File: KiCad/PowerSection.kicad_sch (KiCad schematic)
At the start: 0 parts

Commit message: Partition schematic to different sheets
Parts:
- added C1, C11, C12, C2, C3, C4, C5, C6, C7: C, symbol Device:C
- added D1: 1N5819, Diode_THT:D_DO-41_SOD81_P10.16mm_Horizontal, symbol Diode:1N5819
- added L1: L, symbol Device:L
- added R1, R2, R3: R, symbol Device:R
- added U2: LM7805_TO220, Package_TO_SOT_THT:TO-220-3_Vertical, symbol Regulator_Linear:LM7805_TO220
- added U4: LM7910_TO220, Package_TO_SOT_THT:TO-220-3_Vertical, symbol Regulator_Linear:LM7910_TO220
- added U6: MC34063AP, Package_DIP:DIP-8_W7.62mm_Socket_LongPads, symbol Regulator_Switching:MC34063AP
- added U7: LM7810_TO220, Package_TO_SOT_THT:TO-220-3_Vertical, symbol Regulator_Linear:LM7810_TO220
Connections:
- new net: D1.1 (K), L1.1, U6.2 (SwE)
- new net: C4.1, U6.3 (TC)
- new net: R1.2, U6.1 (SwC), U6.7 (Ipk), U6.8 (DC)
- new net: R2.2, R3.1, U6.5 (Vfb)
- new net +10V: C12.1, U7.3 (VO)
- new net +12V: C2.1, C3.1, C7.1, R1.1, U2.1 (VI), U6.6 (Vin), U7.1 (VI)
- new net +5V: C5.1, U2.3 (VO)
- new net -10V: C6.2, U4.3 (VO)
- new net -12V: C1.2, C11.2, C4.2, D1.2 (A), R2.1, U4.2 (VI), U6.4 (GND)
- new net GND: C1.1, C11.1, C12.2, C2.2, C3.2, C5.2, C6.1, C7.2, L1.2, R3.2, U2.2 (GND), U4.1 (GND), U7.2 (GND)
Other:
- note added: "5V Logic Stabilizer"
- note added: "Author:"
- note added: "Blazej Chodorowski"
- note added: "Invrting DC-DC coverter"
- note added: "Negative Supply Stabilizer"
- note added: "Positive Supply Stabilizer"
- note added: "Power convertion and stabilization module"

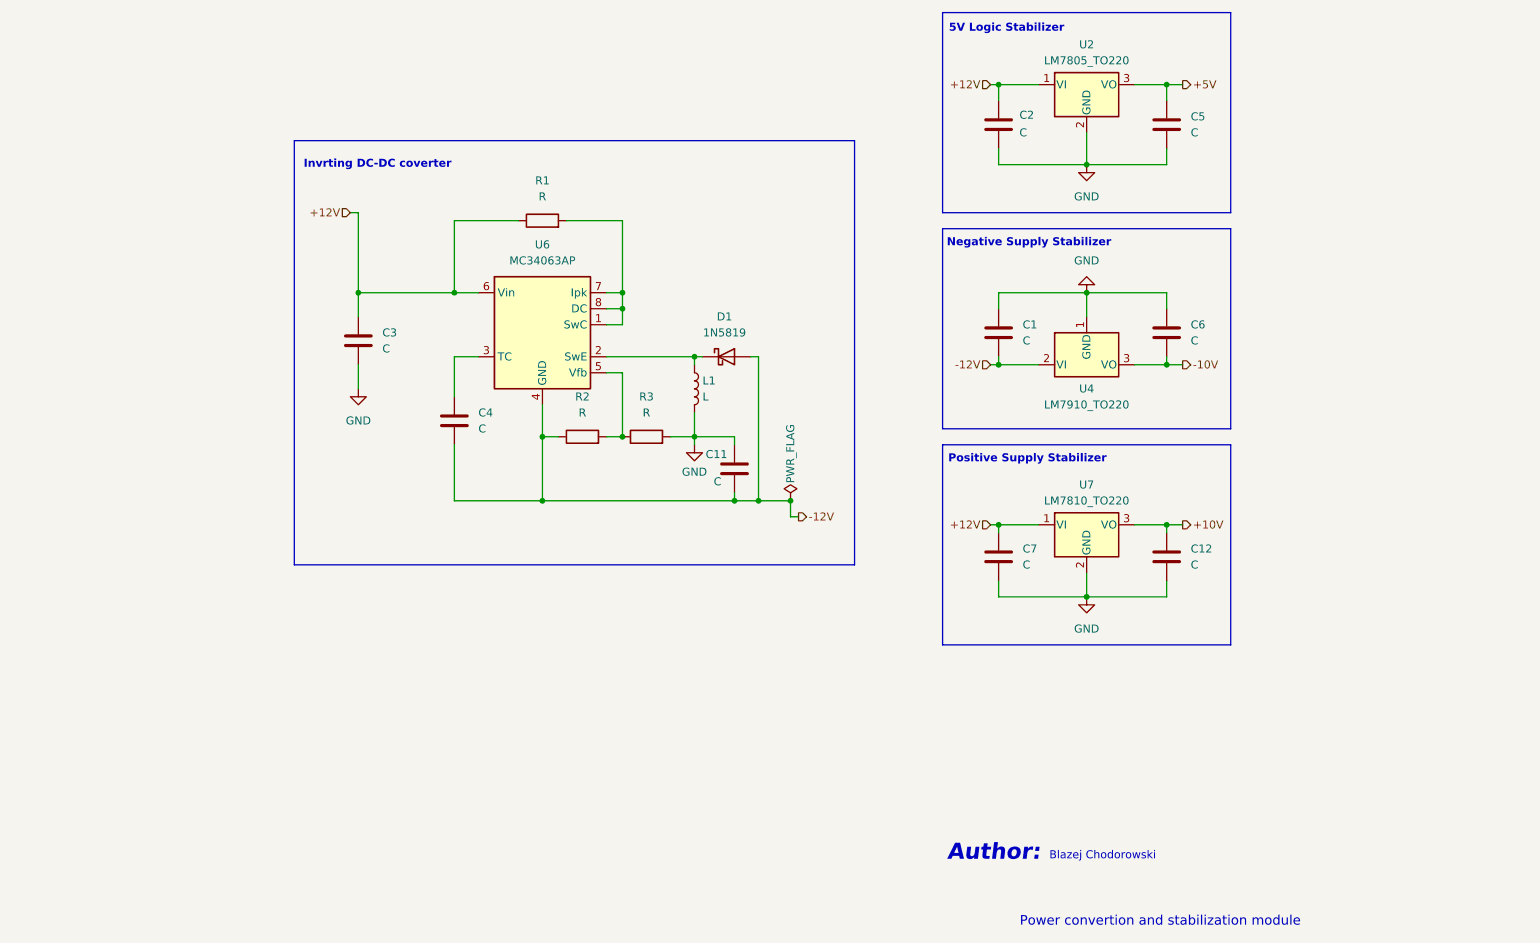
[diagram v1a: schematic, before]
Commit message: Added elements values
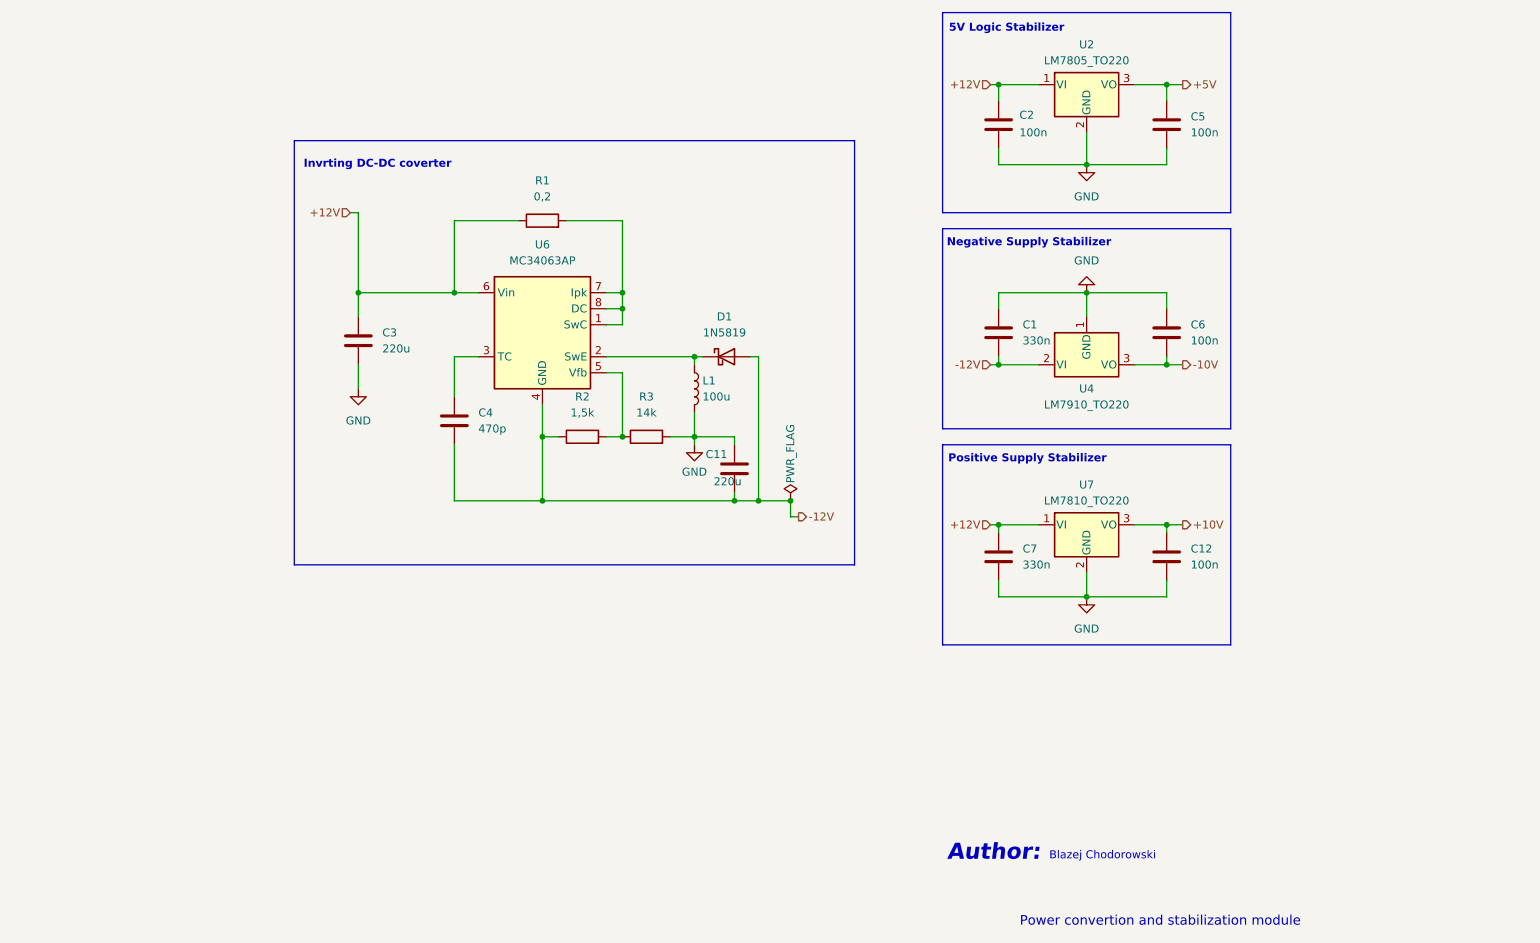
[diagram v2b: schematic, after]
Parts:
- C1, C7: value C -> 330n
- C11, C3: value C -> 220u
- C12, C2, C5, C6: value C -> 100n
- C4: value C -> 470p
- L1: value L -> 100u
- R1: value R -> 0,2
- R2: value R -> 1,5k
- R3: value R -> 14k
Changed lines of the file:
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@@
 			)
 		)
-		(property "Value" "C"
+		(property "Value" "100n"
 			(at 215.9 97.7899 0)
 			(effects
@@
 			)
 		)
-		(property "Value" "L"
+		(property "Value" "100u"
 			(at 138.43 106.6799 0)
 			(effects
@@
 			)
 		)
-		(property "Value" "C"
+		(property "Value" "330n"
 			(at 189.23 97.7899 0)
 			(effects
@@
 			)
 		)
-		(property "Value" "C"
+		(property "Value" "470p"
 			(at 102.87 111.7599 0)
 			(effects
@@
 			)
 		)
-		(property "Value" "C"
+		(property "Value" "330n"
 			(at 189.23 133.3499 0)
 			(effects
@@
 			)
 		)
-		(property "Value" "R"
+		(property "Value" "14k"
 			(at 129.54 109.22 90)
 			(effects
@@
 			)
 		)
-		(property "Value" "C"
+		(property "Value" "100n"
 			(at 215.9 64.7699 0)
 			(effects
@@
 			)
 		)
-		(property "Value" "C"
+		(property "Value" "220u"
 			(at 87.63 99.0599 0)
 			(effects
@@
 			)
 		)
-		(property "Value" "R"
+		(property "Value" "0,2"
 			(at 113.03 74.93 90)
 			(effects
@@
 			)
 		)
-		(property "Value" "C"
+		(property "Value" "100n"
 			(at 215.9 133.3499 0)
 			(effects
@@
 			)
 		)
-		(property "Value" "C"
+		(property "Value" "100n"
 			(at 188.722 64.77 0)
 			(effects
@@
 			)
 		)
-		(property "Value" "R"
+		(property "Value" "1,5k"
 			(at 119.38 109.22 90)
 			(effects
@@
 			)
 		)
-		(property "Value" "C"
+		(property "Value" "220u"
 			(at 140.208 120.142 0)
 			(effects

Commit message: Filled in schematic
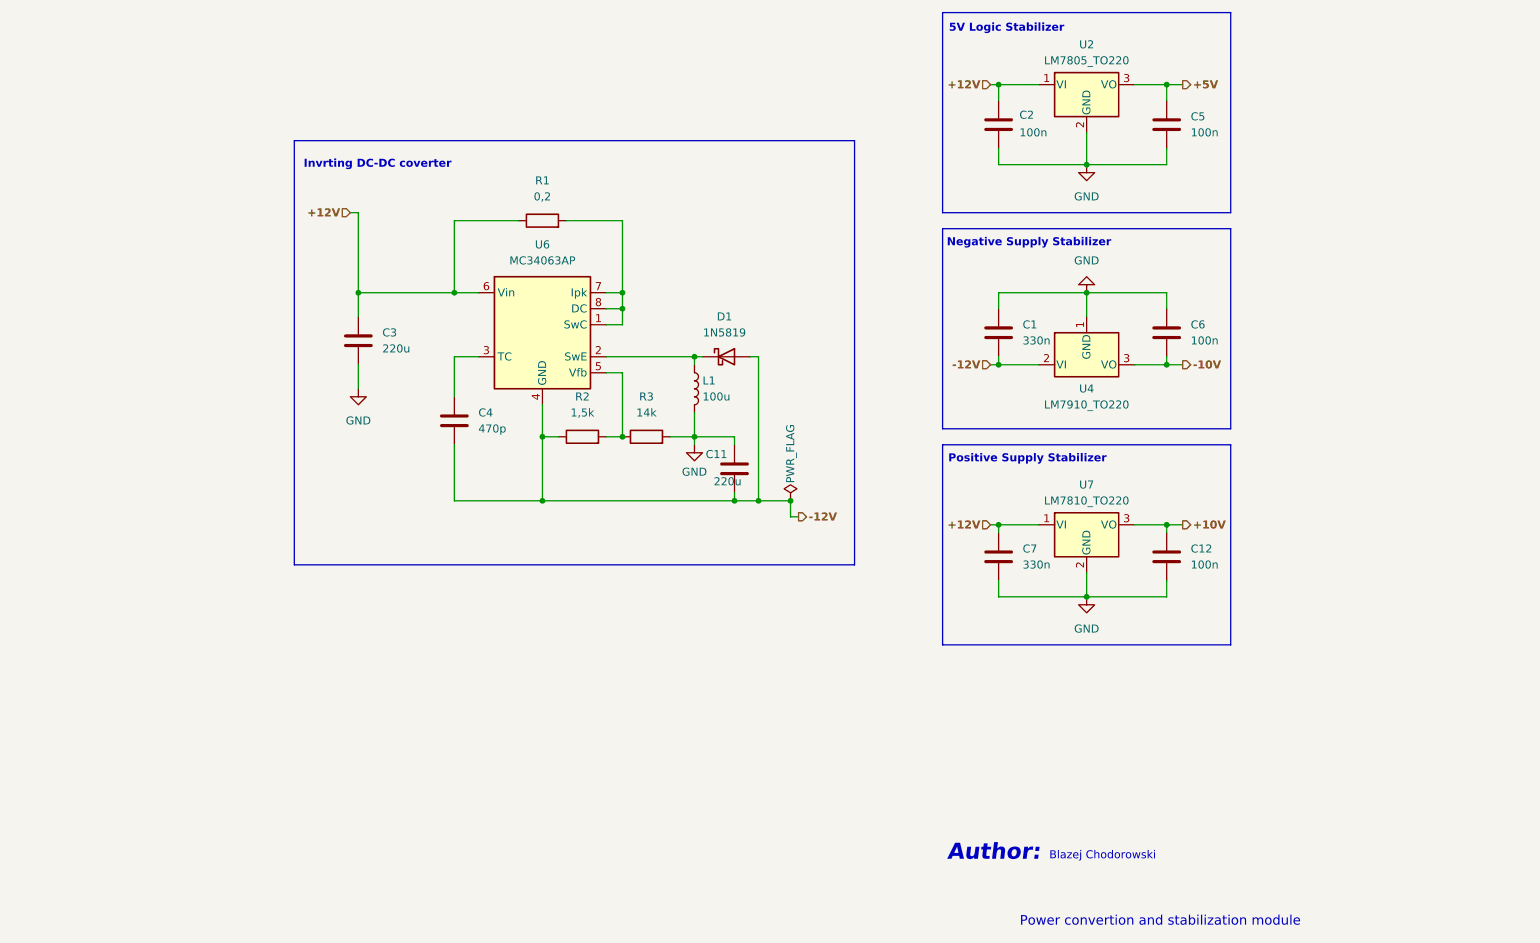
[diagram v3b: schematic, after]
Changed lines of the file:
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@@
 			(font
 				(size 1.27 1.27)
+				(thickness 0.254)
+				(bold yes)
 			)
 			(justify right)
@@
 			(font
 				(size 1.27 1.27)
+				(thickness 0.254)
+				(bold yes)
 			)
 			(justify left)
@@
 			(font
 				(size 1.27 1.27)
+				(thickness 0.254)
+				(bold yes)
 			)
 			(justify right)
@@
 			(font
 				(size 1.27 1.27)
+				(thickness 0.254)
+				(bold yes)
 			)
 			(justify left)
@@
 			(font
 				(size 1.27 1.27)
+				(thickness 0.254)
+				(bold yes)
 			)
 			(justify right)
@@
 			(font
 				(size 1.27 1.27)
+				(thickness 0.254)
+				(bold yes)
 			)
 			(justify left)
@@
 			(font
 				(size 1.27 1.27)
+				(thickness 0.254)
+				(bold yes)
 			)
 			(justify right)
@@
 			(font
 				(size 1.27 1.27)
+				(thickness 0.254)
+				(bold yes)
 			)
 			(justify left)

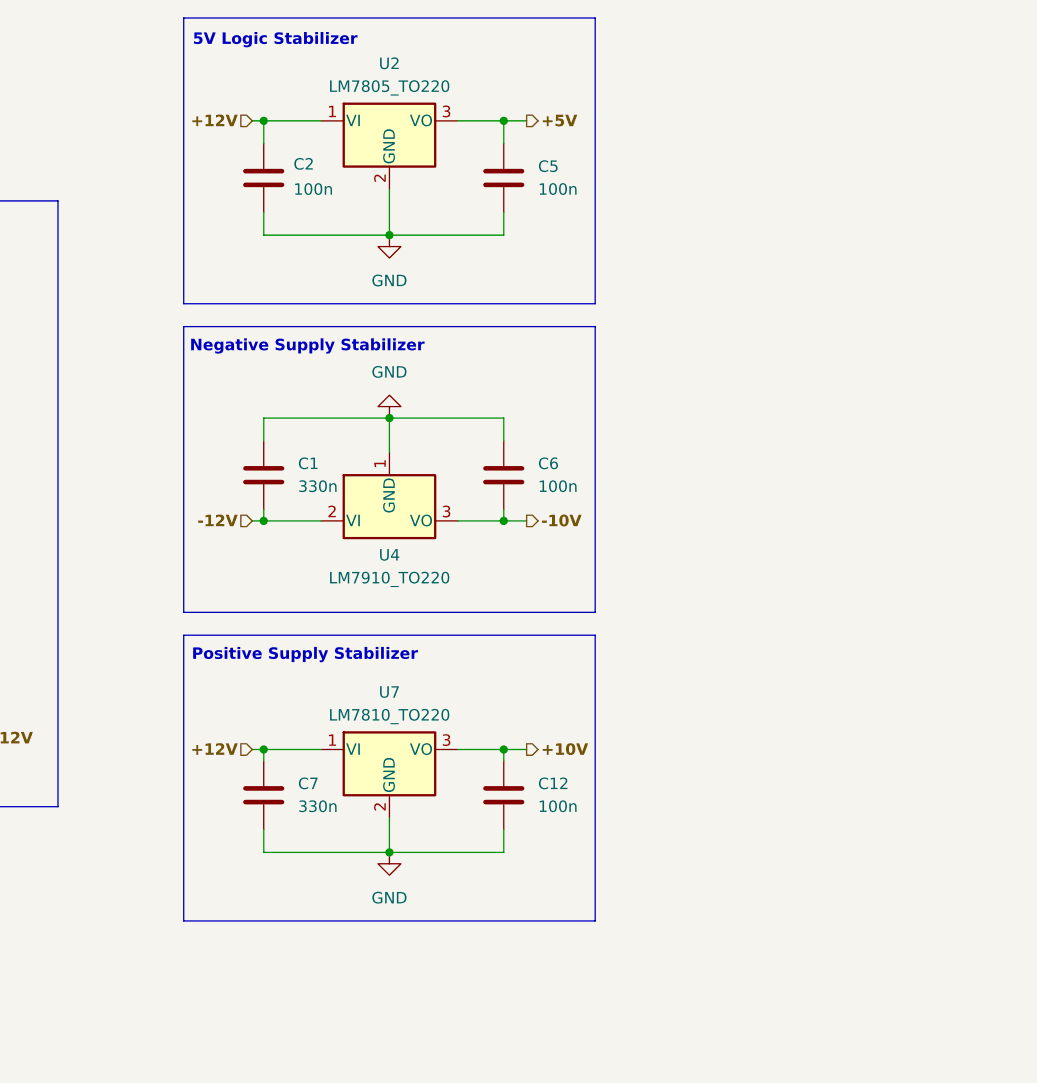
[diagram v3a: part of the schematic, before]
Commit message: Added footprints
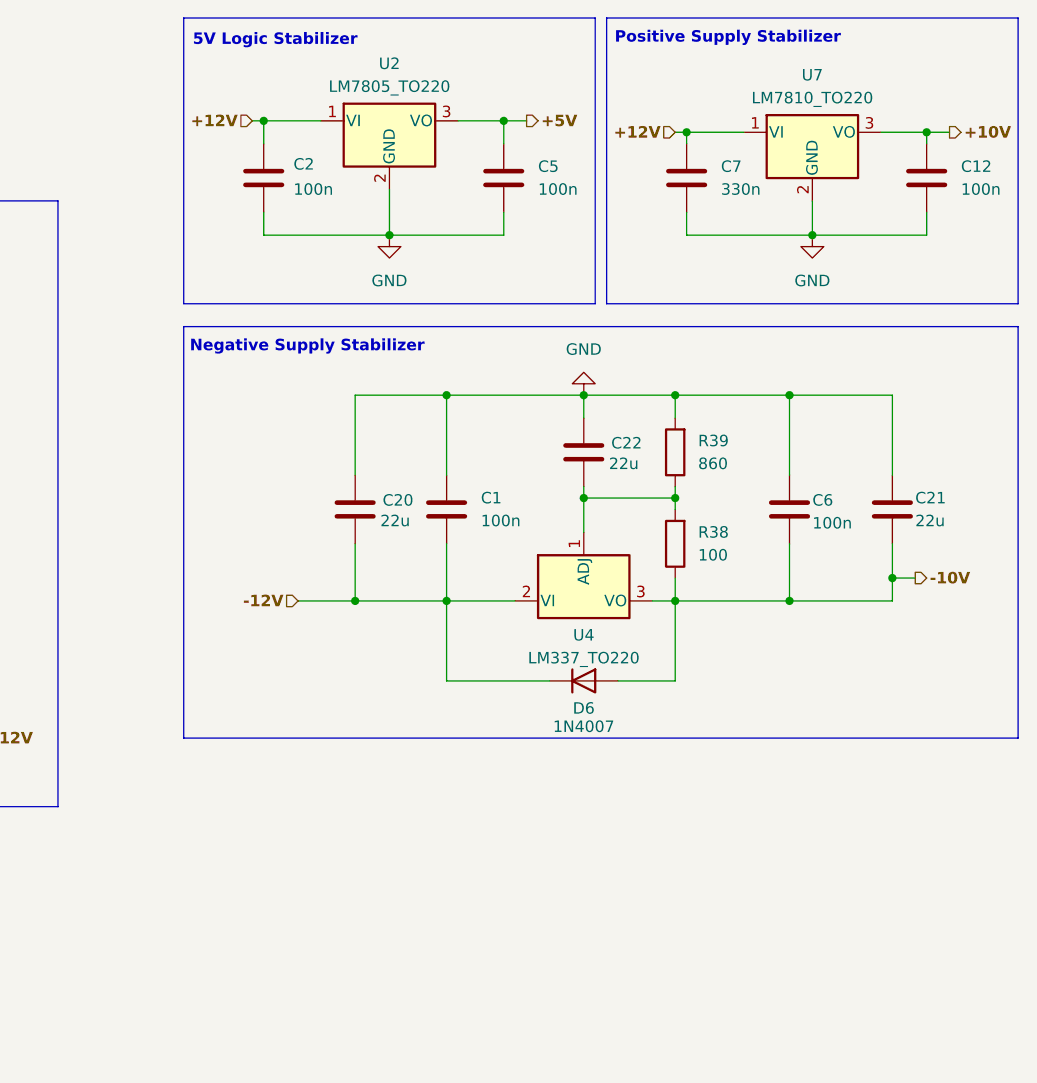
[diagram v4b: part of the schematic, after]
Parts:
- removed U4: LM7910_TO220, Package_TO_SOT_THT:TO-220-3_Vertical, symbol Regulator_Linear:LM7910_TO220
- added C20, C21, C22: 22u, Capacitor_SMD:CP_Elec_6.3x5.3, symbol Device:C
- added D6: 1N4007, Diode_THT:D_DO-41_SOD81_P10.16mm_Horizontal, symbol Diode:1N4007
- added R38: 100, Resistor_SMD:R_0805_2012Metric_Pad1.20x1.40mm_HandSolder, symbol Device:R
- added R39: 860, Resistor_SMD:R_0805_2012Metric_Pad1.20x1.40mm_HandSolder, symbol Device:R
- added U4: LM337_TO220, Package_TO_SOT_THT:TO-220-3_Vertical, symbol Regulator_Linear:LM337_TO220
- C1: value 330n -> 100n; footprint (none) -> Capacitor_SMD:C_0805_2012Metric_Pad1.18x1.45mm_HandSolder
- C11, C3: footprint (none) -> Capacitor_SMD:CP_Elec_6.3x7.7
- C12, C2, C4, C5, C6, C7: footprint (none) -> Capacitor_SMD:C_0805_2012Metric_Pad1.18x1.45mm_HandSolder
- L1: footprint (none) -> Inductor_THT:L_Radial_D8.7mm_P5.00mm_Fastron_07HCP
- R1, R2, R3: footprint (none) -> Resistor_SMD:R_0805_2012Metric_Pad1.20x1.40mm_HandSolder
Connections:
- net -10V: now also C21.2, D6.2 (A), R38.1, U4.3 (VO)
- net -12V: now also C20.2, D6.1 (K), U4.2 (VI)
- net GND: now also C20.1, C21.1, C22.1, R39.2
- new net: C22.2, R38.2, R39.1, U4.1 (ADJ)
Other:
- moved on the sheet: C1, C12, C6, C7, U7

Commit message: minor changes
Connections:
- net -10V: now also D6.1 (K); no longer D6.2 (A)
- net -12V: now also D6.2 (A); no longer D6.1 (K)
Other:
- note added: "5V MCU Pwr Stabilizer"
- note removed: "5V Logic Stabilizer"
- moved on the sheet: C1, C11, C12, C2, C20, C21, C22, C3, C4, C5, C6, C7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
